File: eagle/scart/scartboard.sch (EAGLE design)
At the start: 42 parts, among them Q1 BC548-TO92-E1-REV, Q2 BC548-TO92-E1-REV, Q3 BC548-TO92-E1-REV, Q4 BC548-TO92-E1-REV, T1 BSS138, T3 BSS138, X1 SCART-F

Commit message: WIP
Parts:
- Q2: value BC548-TO92-E1-REV -> BC548; device bc548:BC548-TO92-E1-REV -> transistor-npn:BC548
- R8: value 1000 -> 75
- R9: value 1000 -> 750
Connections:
- new net VCC_CORE: SV8.1, SV8.3
- net ALEFT: now also JP4.6; no longer JP4.4
- net ARIGHT: now also JP4.4; no longer JP4.6
- net VCC_B0: now also SV8.7
- net VCC_B1: now also SV8.11
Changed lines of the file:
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@@
 </variantdefs>
 <classes>
-<class number="0" name="default" width="0" drill="0">
+<class number="0" name="default" width="0.2" drill="1.1">
+<clearance class="0" value="0.2"/>
 </class>
 <class number="1" name="power" width="0.6" drill="1.1">
@@
 <part name="R33" library="rcl" deviceset="R-EU_" device="R0805" value="4700"/>
 <part name="Q1" library="bc548" deviceset="BC548*" device="-TO92-E1-REV"/>
-<part name="Q2" library="bc548" deviceset="BC548*" device="-TO92-E1-REV"/>
 <part name="Q3" library="bc548" deviceset="BC548*" device="-TO92-E1-REV"/>
 <part name="Q4" library="bc548" deviceset="BC548*" device="-TO92-E1-REV"/>
-<part name="R8" library="rcl" deviceset="R-EU_" device="R0805" value="1000"/>
-<part name="R9" library="rcl" deviceset="R-EU_" device="R0805" value="1000"/>
+<part name="R8" library="rcl" deviceset="R-EU_" device="R0805" value="75"/>
+<part name="R9" library="rcl" deviceset="R-EU_" device="R0805" value="750"/>
 <part name="R10" library="rcl" deviceset="R-EU_" device="R0805" value="1000"/>
 <part name="R11" library="rcl" deviceset="R-EU_" device="R0805" value="1000"/>
 <part name="JP4" library="pinhead" deviceset="PINHD-2X3" device=""/>
+<part name="Q2" library="transistor-npn" deviceset="BC548*" device=""/>
 </parts>
 <sheets>
@@
 <instance part="R33" gate="G$1" x="-12.7" y="-111.76" rot="R90"/>
 <instance part="Q1" gate="G$1" x="-20.32" y="-50.8"/>
-<instance part="Q2" gate="G$1" x="-20.32" y="-20.32"/>
 <instance part="Q3" gate="G$1" x="-20.32" y="-76.2"/>
 <instance part="Q4" gate="G$1" x="-20.32" y="-101.6"/>
@@
 <instance part="R11" gate="G$1" x="40.64" y="-38.1"/>
 <instance part="JP4" gate="A" x="25.4" y="-33.02" rot="R180"/>
+<instance part="Q2" gate="G$1" x="-20.32" y="-20.32"/>
 </instances>
 <busses>
@@
 </segment>
 <segment>
+<pinref part="JP4" gate="A" pin="4"/>
+<wire x1="12.7" y1="-33.02" x2="20.32" y2="-33.02" width="0.1524" layer="91"/>
+<label x="12.7" y="-33.02" size="1.778" layer="95"/>
+</segment>
+</net>
+<net name="ALEFT" class="0">
+<segment>
+<pinref part="X1" gate="G$1" pin="6"/>
+<wire x1="45.72" y1="30.48" x2="53.34" y2="30.48" width="0.1524" layer="91"/>
+<label x="55.88" y="30.48" size="1.778" layer="95"/>
+</segment>
+<segment>
 <pinref part="JP4" gate="A" pin="6"/>
 <wire x1="20.32" y1="-30.48" x2="12.7" y2="-30.48" width="0.1524" layer="91"/>
 <label x="12.7" y="-30.48" size="1.778" layer="95"/>
-</segment>
-</net>
-<net name="ALEFT" class="0">
-<segment>
-<pinref part="X1" gate="G$1" pin="6"/>
-<wire x1="45.72" y1="30.48" x2="53.34" y2="30.48" width="0.1524" layer="91"/>
-<label x="55.88" y="30.48" size="1.778" layer="95"/>
-</segment>
-<segment>
-<pinref part="JP4" gate="A" pin="4"/>
-<wire x1="12.7" y1="-33.02" x2="20.32" y2="-33.02" width="0.1524" layer="91"/>
-<label x="12.7" y="-33.02" size="1.778" layer="95"/>
 </segment>
 </net>
@@
 <segment>
 <pinref part="X1" gate="G$1" pin="8"/>
-<wire x1="45.72" y1="35.56" x2="53.34" y2="35.56" width="0.1524" layer="91"/>
+<wire x1="45.72" y1="35.56" x2="50.8" y2="35.56" width="0.1524" layer="91"/>
 <label x="55.88" y="35.56" size="1.778" layer="95"/>
+<wire x1="50.8" y1="35.56" x2="53.34" y2="35.56" width="0.1524" layer="91"/>
+<wire x1="53.34" y1="45.72" x2="50.8" y2="43.18" width="0.1524" layer="91"/>
+<wire x1="50.8" y1="43.18" x2="50.8" y2="35.56" width="0.1524" layer="91"/>
+<junction x="50.8" y="35.56"/>
 </segment>
 </net>
@@
 <net name="VCC_CORE" class="0">
 <segment>
-<wire x1="200.66" y1="55.88" x2="203.2" y2="55.88" width="0.1524" layer="91"/>
 <label x="200.66" y="50.8" size="1.778" layer="95" rot="R270"/>
-<wire x1="200.66" y1="55.88" x2="200.66" y2="50.8" width="0.1524" layer="91"/>
+<pinref part="SV8" gate="G$1" pin="3"/>
+<wire x1="200.66" y1="53.34" x2="200.66" y2="50.8" width="0.1524" layer="91"/>
+<wire x1="203.2" y1="55.88" x2="203.2" y2="53.34" width="0.1524" layer="91"/>
+<wire x1="203.2" y1="53.34" x2="200.66" y2="53.34" width="0.1524" layer="91"/>
+<pinref part="SV8" gate="G$1" pin="1"/>
+<wire x1="200.66" y1="55.88" x2="200.66" y2="53.34" width="0.1524" layer="91"/>
+<junction x="200.66" y="53.34"/>
 </segment>
 </net>
 <net name="VCC_B0" class="0">
 <segment>
-<wire x1="208.28" y1="55.88" x2="205.74" y2="55.88" width="0.1524" layer="91"/>
 <label x="204.724" y="50.292" size="1.778" layer="95" rot="R270"/>
 <pinref part="SV8" gate="G$1" pin="5"/>
-<wire x1="205.74" y1="55.88" x2="205.74" y2="50.8" width="0.1524" layer="91"/>
-<junction x="205.74" y="55.88"/>
+<wire x1="205.74" y1="55.88" x2="205.74" y2="53.34" width="0.1524" layer="91"/>
+<pinref part="SV8" gate="G$1" pin="7"/>
+<wire x1="205.74" y1="53.34" x2="205.74" y2="50.8" width="0.1524" layer="91"/>
+<wire x1="208.28" y1="55.88" x2="208.28" y2="53.34" width="0.1524" layer="91"/>
+<wire x1="208.28" y1="53.34" x2="205.74" y2="53.34" width="0.1524" layer="91"/>
+<junction x="205.74" y="53.34"/>
 </segment>
 </net>
@@
 <segment>
 <label x="210.82" y="50.8" size="1.778" layer="95" rot="R270"/>
-<wire x1="210.82" y1="55.88" x2="213.36" y2="55.88" width="0.1524" layer="91"/>
 <pinref part="SV8" gate="G$1" pin="9"/>
-<junction x="210.82" y="55.88"/>
-<wire x1="210.82" y1="55.88" x2="210.82" y2="50.8" width="0.1524" layer="91"/>
+<wire x1="210.82" y1="55.88" x2="210.82" y2="53.34" width="0.1524" layer="91"/>
+<pinref part="SV8" gate="G$1" pin="11"/>
+<wire x1="210.82" y1="53.34" x2="210.82" y2="50.8" width="0.1524" layer="91"/>
+<wire x1="213.36" y1="55.88" x2="213.36" y2="53.34" width="0.1524" layer="91"/>
+<wire x1="213.36" y1="53.34" x2="210.82" y2="53.34" width="0.1524" layer="91"/>
+<junction x="210.82" y="53.34"/>
 </segment>
 </net>
@@
 <label x="48.26" y="-43.18" size="1.778" layer="95"/>
 </segment>
+<segment>
+<wire x1="68.58" y1="45.72" x2="71.12" y2="45.72" width="0.1524" layer="91"/>
+<label x="71.12" y="45.72" size="1.778" layer="95"/>
+</segment>
 </net>
 <net name="B_SPARE" class="0">
@@
 </segment>
 </net>
-<net name="N$3" class="0">
-<segment>
-<pinref part="R5" gate="G$1" pin="2"/>
-<pinref part="Q2" gate="G$1" pin="B"/>
-</segment>
-</net>
 <net name="N$4" class="0">
 <segment>
@@
 </segment>
 </net>
+<net name="N$3" class="0">
+<segment>
+<pinref part="R5" gate="G$1" pin="2"/>
+<pinref part="Q2" gate="G$1" pin="B"/>
+</segment>
+</net>

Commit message: WIP
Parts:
- added IC1: 25LC080SN, microchip:25LC080SN
- added JP5: (no value), jumper:JP2E
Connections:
- new net N$7: IC1.!WP, JP5.2
- net GND: now also IC1.GND, JP5.3
- net SPI_CLK: now also IC1.SCK, SV8.8; no longer SV8.6
- net SPI_DI: now also IC1.SI, SV8.6; no longer SV8.8
- net SPI_DO: now also IC1.SO
- net SPI_SEL0: now also IC1.!CS
- net VCC_B0: now also IC1.!HOLD, IC1.VCC, JP5.1
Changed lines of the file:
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@@
 <part name="JP4" library="pinhead" deviceset="PINHD-2X3" device=""/>
 <part name="Q2" library="transistor-npn" deviceset="BC548*" device=""/>
+<part name="IC1" library="microchip" deviceset="25*" device="SN" technology="LC080"/>
+<part name="JP5" library="jumper" deviceset="JP2E" device=""/>
 </parts>
 <sheets>
@@
 <instance part="JP4" gate="A" x="25.4" y="-33.02" rot="R180"/>
 <instance part="Q2" gate="G$1" x="-20.32" y="-20.32"/>
+<instance part="IC1" gate="G$1" x="203.2" y="114.3"/>
+<instance part="JP5" gate="1" x="172.72" y="121.92" rot="R90"/>
 </instances>
 <busses>
@@
 <net name="SPI_CLK" class="0">
 <segment>
+<pinref part="IC1" gate="G$1" pin="SCK"/>
+<wire x1="182.88" y1="111.76" x2="190.5" y2="111.76" width="0.1524" layer="91"/>
+<label x="182.88" y="111.76" size="1.778" layer="95"/>
+</segment>
+<segment>
+<wire x1="208.28" y1="71.12" x2="208.28" y2="73.66" width="0.1524" layer="91"/>
+<label x="208.28" y="73.66" size="1.778" layer="95" rot="R90"/>
+<pinref part="SV8" gate="G$1" pin="8"/>
+</segment>
+</net>
+<net name="SPI_DI" class="0">
+<segment>
+<pinref part="IC1" gate="G$1" pin="SI"/>
+<wire x1="182.88" y1="114.3" x2="190.5" y2="114.3" width="0.1524" layer="91"/>
+<label x="182.88" y="114.3" size="1.778" layer="95"/>
+</segment>
+<segment>
 <wire x1="205.74" y1="73.66" x2="205.74" y2="71.12" width="0.1524" layer="91"/>
 <label x="205.74" y="73.66" size="1.778" layer="95" rot="R90"/>
@@
 </segment>
 </net>
-<net name="SPI_DI" class="0">
-<segment>
-<wire x1="208.28" y1="71.12" x2="208.28" y2="73.66" width="0.1524" layer="91"/>
-<label x="208.28" y="73.66" size="1.778" layer="95" rot="R90"/>
-<pinref part="SV8" gate="G$1" pin="8"/>
-</segment>
-</net>
 <net name="SPI_SEL1" class="0">
 <segment>
@@
 <pinref part="SV8" gate="G$1" pin="4"/>
 </segment>
+<segment>
+<pinref part="IC1" gate="G$1" pin="SO"/>
+<wire x1="223.52" y1="114.3" x2="218.44" y2="114.3" width="0.1524" layer="91"/>
+<label x="218.44" y="114.3" size="1.778" layer="95"/>
+</segment>
 </net>
 <net name="SPI_SEL0" class="0">
@@
 <label x="200.66" y="73.66" size="1.778" layer="95" rot="R90"/>
 <pinref part="SV8" gate="G$1" pin="2"/>
+</segment>
+<segment>
+<pinref part="IC1" gate="G$1" pin="!CS"/>
+<wire x1="182.88" y1="116.84" x2="190.5" y2="116.84" width="0.1524" layer="91"/>
+<label x="182.88" y="116.84" size="1.778" layer="95"/>
 </segment>
 </net>
@@
 <wire x1="208.28" y1="53.34" x2="205.74" y2="53.34" width="0.1524" layer="91"/>
 <junction x="205.74" y="53.34"/>
+</segment>
+<segment>
+<pinref part="IC1" gate="G$1" pin="VCC"/>
+<wire x1="210.82" y1="127" x2="223.52" y2="127" width="0.1524" layer="91"/>
+<label x="218.44" y="127" size="1.778" layer="95"/>
+</segment>
+<segment>
+<pinref part="IC1" gate="G$1" pin="!HOLD"/>
+<label x="182.88" y="109.22" size="1.778" layer="95"/>
+<wire x1="175.26" y1="119.38" x2="175.26" y2="109.22" width="0.1524" layer="91"/>
+<wire x1="175.26" y1="109.22" x2="190.5" y2="109.22" width="0.1524" layer="91"/>
+<pinref part="JP5" gate="1" pin="1"/>
 </segment>
 </net>
@@
 <label x="71.12" y="45.72" size="1.778" layer="95"/>
 </segment>
+<segment>
+<pinref part="IC1" gate="G$1" pin="GND"/>
+<wire x1="223.52" y1="104.14" x2="213.36" y2="104.14" width="0.1524" layer="91"/>
+<label x="218.44" y="104.14" size="1.778" layer="95"/>
+<wire x1="213.36" y1="104.14" x2="210.82" y2="104.14" width="0.1524" layer="91"/>
+<wire x1="213.36" y1="104.14" x2="213.36" y2="99.06" width="0.1524" layer="91"/>
+<junction x="213.36" y="104.14"/>
+<wire x1="213.36" y1="99.06" x2="167.64" y2="99.06" width="0.1524" layer="91"/>
+<wire x1="167.64" y1="99.06" x2="167.64" y2="127" width="0.1524" layer="91"/>
+<wire x1="167.64" y1="127" x2="177.8" y2="127" width="0.1524" layer="91"/>
+<wire x1="177.8" y1="127" x2="177.8" y2="124.46" width="0.1524" layer="91"/>
+<pinref part="JP5" gate="1" pin="3"/>
+<wire x1="177.8" y1="124.46" x2="175.26" y2="124.46" width="0.1524" layer="91"/>
+</segment>
 </net>
 <net name="B_SPARE" class="0">
@@
 </segment>
 </net>
+<net name="N$7" class="0">
+<segment>
+<pinref part="IC1" gate="G$1" pin="!WP"/>
+<wire x1="175.26" y1="121.92" x2="190.5" y2="121.92" width="0.1524" layer="91"/>
+<pinref part="JP5" gate="1" pin="2"/>
+</segment>
+</net>

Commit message: WIP
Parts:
- added C1: (no value), rcl:C-EUC0603
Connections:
- net GND: now also C1.1
- net VCC_B0: now also C1.2
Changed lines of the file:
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@@
 <part name="IC1" library="microchip" deviceset="25*" device="SN" technology="LC080"/>
 <part name="JP5" library="jumper" deviceset="JP2E" device=""/>
+<part name="C1" library="rcl" deviceset="C-EU" device="C0603"/>
 </parts>
 <sheets>
@@
 <instance part="IC1" gate="G$1" x="203.2" y="114.3"/>
 <instance part="JP5" gate="1" x="172.72" y="121.92" rot="R90"/>
+<instance part="C1" gate="G$1" x="88.9" y="127" rot="R180"/>
 </instances>
 <busses>
@@
 <wire x1="175.26" y1="109.22" x2="190.5" y2="109.22" width="0.1524" layer="91"/>
 <pinref part="JP5" gate="1" pin="1"/>
+</segment>
+<segment>
+<pinref part="C1" gate="G$1" pin="2"/>
+<wire x1="88.9" y1="132.08" x2="78.74" y2="132.08" width="0.1524" layer="91"/>
+<label x="78.74" y="132.08" size="1.778" layer="95"/>
 </segment>
 </net>
@@
 <wire x1="177.8" y1="124.46" x2="175.26" y2="124.46" width="0.1524" layer="91"/>
 </segment>
-</net>
+<segment>
+<pinref part="C1" gate="G$1" pin="1"/>
+<wire x1="78.74" y1="124.46" x2="88.9" y2="124.46" width="0.1524" layer="91"/>
+<label x="78.74" y="124.46" size="1.778" layer="95"/>
+</segment>
+</net>

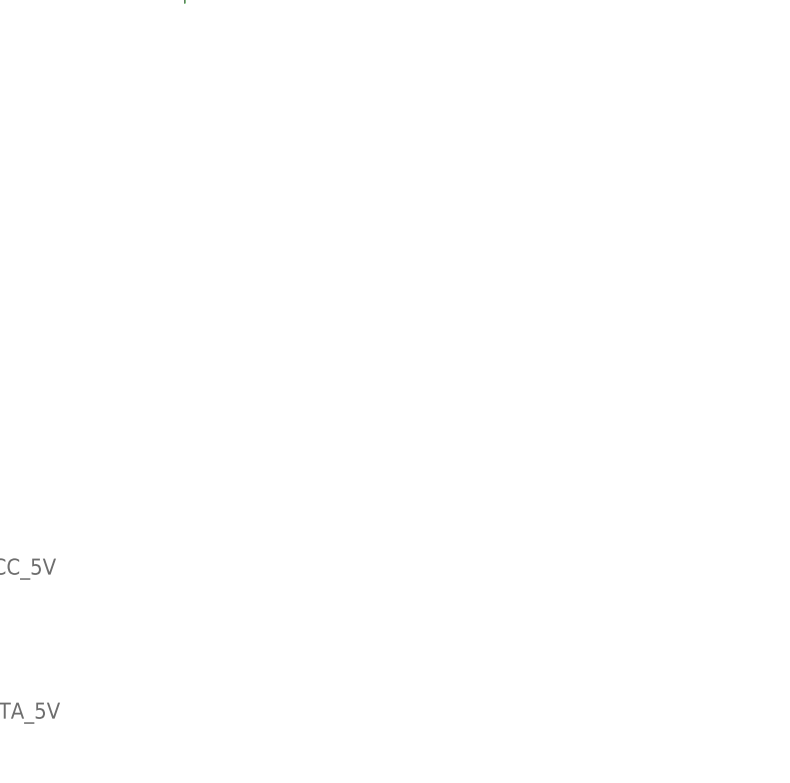
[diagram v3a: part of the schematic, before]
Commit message: reworked scart board... not yet etched and tested
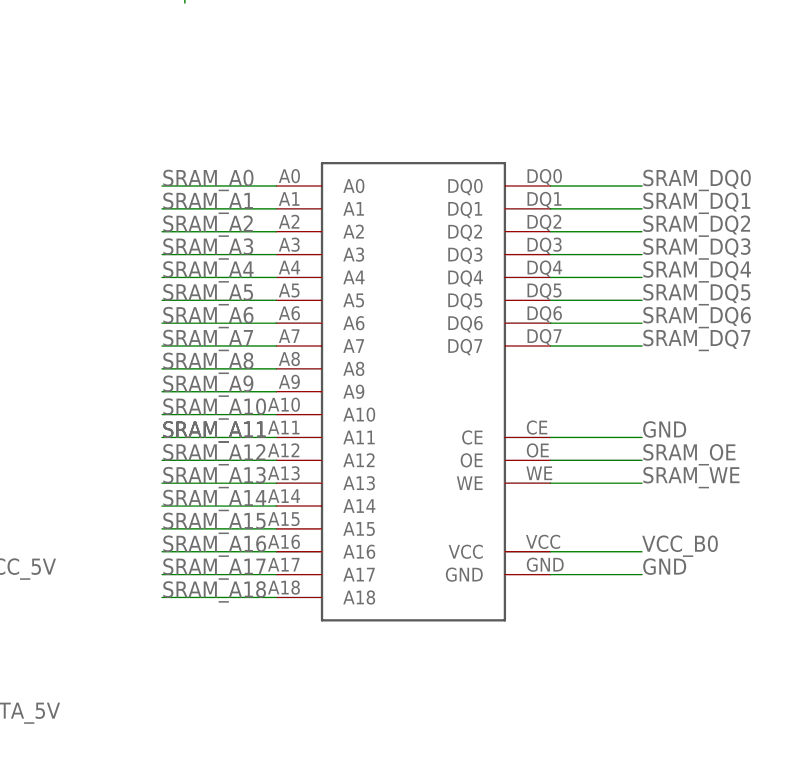
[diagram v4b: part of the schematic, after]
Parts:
- added U$1: AS6C4008, sram:AS6C4008
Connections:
- net GND: now also U$1.CE, U$1.GND
- net SRAM_A0: now also U$1.A0
- net SRAM_A1: now also U$1.A1
- net SRAM_A10: now also U$1.A10
- net SRAM_A11: now also U$1.A11
- net SRAM_A12: now also U$1.A12
- net SRAM_A13: now also U$1.A13
- net SRAM_A14: now also U$1.A14
- net SRAM_A15: now also U$1.A15
- net SRAM_A16: now also U$1.A16
- net SRAM_A17: now also U$1.A17
- net SRAM_A18: now also U$1.A18
- net SRAM_A2: now also U$1.A2
- net SRAM_A3: now also U$1.A3
- net SRAM_A4: now also U$1.A4
- net SRAM_A5: now also U$1.A5
- net SRAM_A6: now also U$1.A6
- net SRAM_A7: now also U$1.A7
- net SRAM_A8: now also U$1.A8
- net SRAM_A9: now also U$1.A9
- net SRAM_DQ0: now also U$1.DQ0
- net SRAM_DQ1: now also U$1.DQ1
- net SRAM_DQ2: now also U$1.DQ2
- net SRAM_DQ3: now also U$1.DQ3
- net SRAM_DQ4: now also U$1.DQ4
- net SRAM_DQ5: now also U$1.DQ5
- net SRAM_DQ6: now also U$1.DQ6
- net SRAM_DQ7: now also U$1.DQ7
- net SRAM_OE: now also U$1.OE
- net SRAM_WE: now also U$1.WE
- net VCC_B0: now also U$1.VCC

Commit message: going to bed
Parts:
- R10, R11: value 1000 -> 560
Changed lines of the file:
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@@
 <part name="R8" library="rcl" deviceset="R-EU_" device="R0805" value="75"/>
 <part name="R9" library="rcl" deviceset="R-EU_" device="R0805" value="750"/>
-<part name="R10" library="rcl" deviceset="R-EU_" device="R0805" value="1000"/>
-<part name="R11" library="rcl" deviceset="R-EU_" device="R0805" value="1000"/>
+<part name="R10" library="rcl" deviceset="R-EU_" device="R0805" value="560"/>
+<part name="R11" library="rcl" deviceset="R-EU_" device="R0805" value="560"/>
 <part name="JP4" library="pinhead" deviceset="PINHD-2X3" device=""/>
 <part name="Q2" library="transistor-npn" deviceset="BC548*" device=""/>
